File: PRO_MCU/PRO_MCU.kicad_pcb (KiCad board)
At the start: 2 copper layers, 18 parts, among them Q1 TN0702, Q2 TN0702, U1 Chassis, U2 ItsyBitsy_NRF52840, U4 Buttons_LED, U5 waveshare_15867

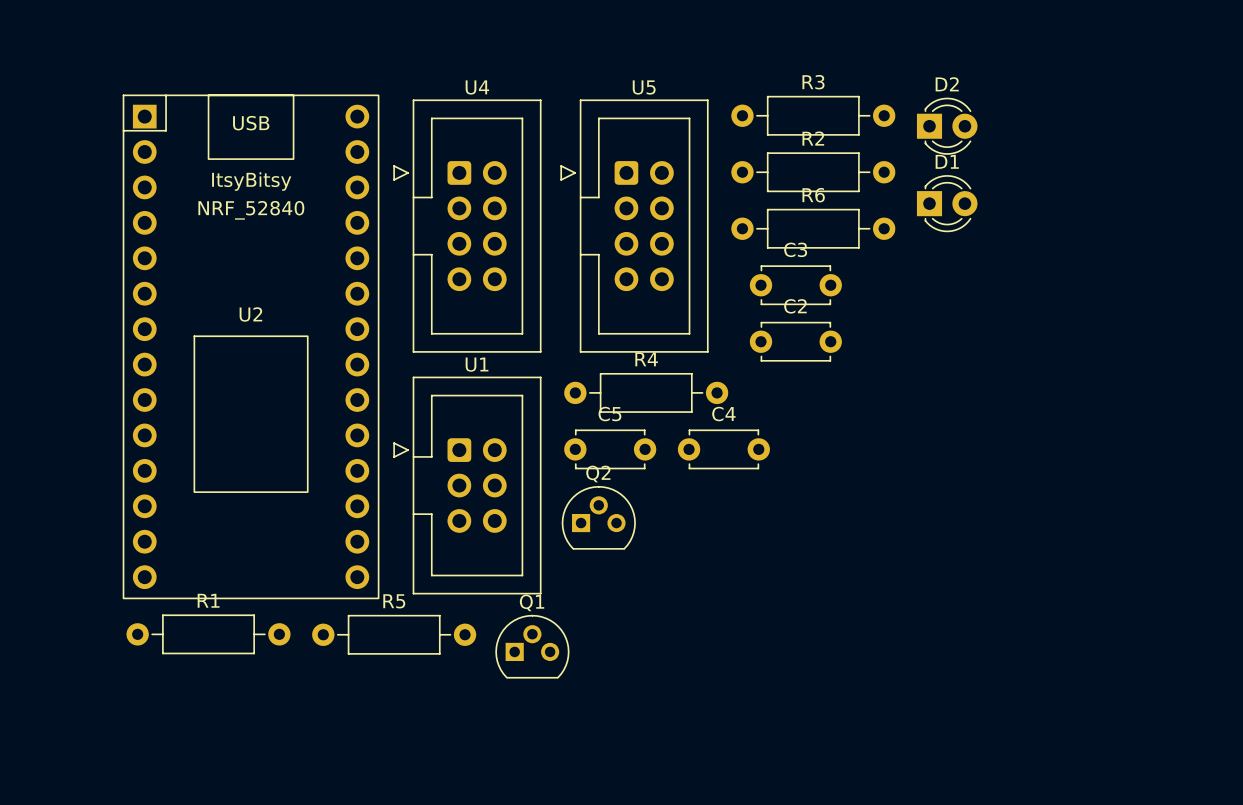
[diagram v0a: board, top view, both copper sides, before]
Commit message: Updates layout, schematic, symbols and footprints
- Adds rounded corners to board geometry
- Component placement
- Modifications to schematic to make routing easier
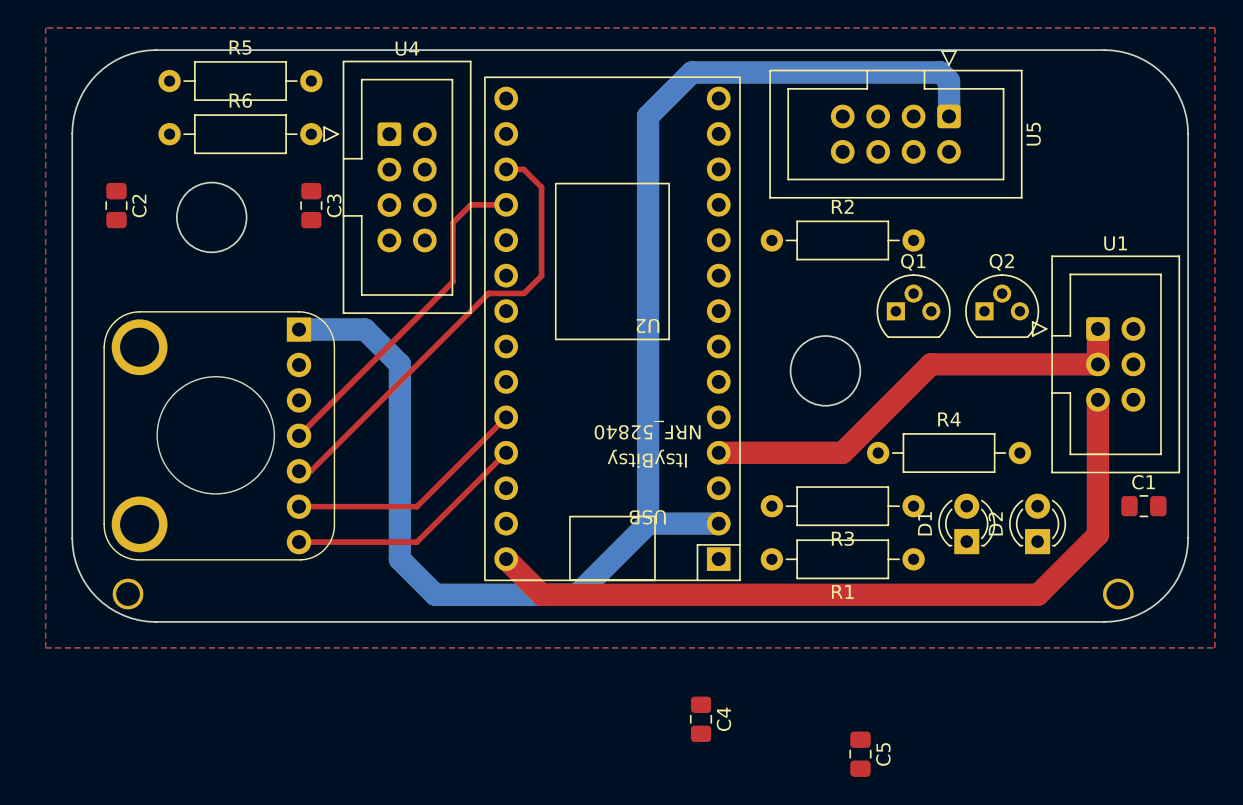
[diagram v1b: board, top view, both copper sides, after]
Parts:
- added C1: 4u7, Capacitor_SMD:C_0805_2012Metric_Pad1.18x1.45mm_HandSolder, F.Cu at (-304.8, 123.2)
- added Logo: BoardGeometry, _PRO_MCU:BoardGeometry, F.Cu at (-341.6, 110.5)
- added U3: MPRLS, PRO_MCU:MPRLS, B.Cu at (-370.8, 118.1)
- C2, C3, C4, C5: footprint Capacitor_THT:C_Disc_D4.7mm_W2.5mm_P5.00mm -> Capacitor_SMD:C_0805_2012Metric_Pad1.18x1.45mm_HandSolder
- moved R1 55.9 mm to (-321.3, 127.0), turned to 180 degrees
- moved C2 47.2 mm to (-378.5, 101.6), turned to -90 degrees
- moved U1 46.6 mm to (-308.1, 110.5)
- moved R6 41.6 mm to (-374.6, 96.5)
- moved R5 41.2 mm to (-374.6, 92.7)
- moved Q1 36.7 mm to (-322.6, 109.2)
- moved C3 32.7 mm to (-364.5, 101.6), turned to -90 degrees
- moved Q2 32.7 mm to (-316.2, 109.2)
- moved D2 30.8 mm to (-312.4, 125.7), turned to 90 degrees
- moved R3 30.6 mm to (-321.3, 123.2), turned to 180 degrees
- moved C5 29.9 mm to (-325.1, 141.0), turned to -90 degrees
- moved D1 24.4 mm to (-317.5, 125.7), turned to 90 degrees
- moved U2 23.7 mm to (-342.9, 111.8), turned to 180 degrees
- moved U5 23.5 mm to (-318.8, 95.2), turned to -90 degrees
- moved R4 22.1 mm to (-323.9, 119.4)
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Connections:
- U2 pad 24: /Valve_Ctrl -> /EOC
- U2 pad 25: /Pump_Ctrl -> /Sensor_RESET
- U2 pad 5: /EOC -> /Valve_Ctrl
- U2 pad 6: /Sensor_RESET -> /Pump_Ctrl
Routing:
- net +3.3V: track 0.00 -> 103.1 mm
- net +BATT: track 0.00 -> 54.9 mm
- net Net-(U2-SDA): track 0.00 -> 32.6 mm
- net VDD: track 0.00 -> 32.4 mm
- net Net-(U2-SCL): track 0.00 -> 24.2 mm
- net /EOC: track 0.00 -> 17.5 mm
- net /Sensor_RESET: track 0.00 -> 17.5 mm
- added copper zone on B.Cu, net GND
- added copper zone on F.Cu, net GND
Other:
- board outline added: 80 x 41 mm

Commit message: V1.0 Fabrication
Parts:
- removed the Logo at (-341.6, 110.5)
- added Logo: BoardGeometry, PRO_MCU:BoardGeometry, F.Cu at (-342.9, 110.5)
- moved C5 46.6 mm to (-311.1, 96.5)
- moved C4 36.4 mm to (-361.3, 111.8)
- moved R4 2.62 mm to (-324.5, 116.8)
- moved C1 1.50 mm to (-306.3, 123.2)
- moved U1 1.27 mm to (-309.4, 110.5)
- moved U3 1.27 mm to (-372.1, 118.1)
- moved Q2 1.27 mm to (-317.5, 109.2)
- moved Q1 0.63 mm to (-323.2, 109.2)
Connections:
- U2 pad 10: /DC -> /CS
- U2 pad 7: /BL -> /DC
- U2 pad 8: /Display_RESET -> /BL
- U2 pad 9: /CS -> /Display_RESET
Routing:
- net /Button_Red: track 0.00 -> 42.7 mm
- net /Button_Green: track 0.00 -> 40.9 mm
- net /Valve_Ctrl: track 0.00 -> 27.4 mm
- net /Valve-: track 0.00 -> 25.2 mm
- net /Led_Green: track 0.00 -> 20.6 mm
- net /MOSI: track 0.00 -> 19.7 mm
- net /DC: track 0.00 -> 19.4 mm
- net /Pump_Ctrl: track 0.00 -> 19.0 mm
- net /CS: track 0.00 -> 18.4 mm
- net /Display_RESET: track 0.00 -> 17.0 mm
- net /SCK: track 0.00 -> 16.7 mm
- net /BL: track 0.00 -> 16.2 mm
- net +3.3V: track 103.1 -> 115.7 mm
- net Net-(D2-A): track 0.00 -> 11.7 mm
- net /Pump-: track 0.00 -> 10.4 mm
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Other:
- outline, holes or cut-outs redrawn
- board text added: "Display"
- board text added: "Front Panel"
- board text added: "Jakob Holz 2023"
- board text added: "Projekt Microcontroller"
- board text added: "Pump"
- board text added: "Universität Ulm"
- board text added: "Valve"
